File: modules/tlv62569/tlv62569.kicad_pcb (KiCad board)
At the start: 2 copper layers, 14.2 x 20.6 mm, 11 parts, among them U1 SMAJ17A, U2 TLV62569DBV

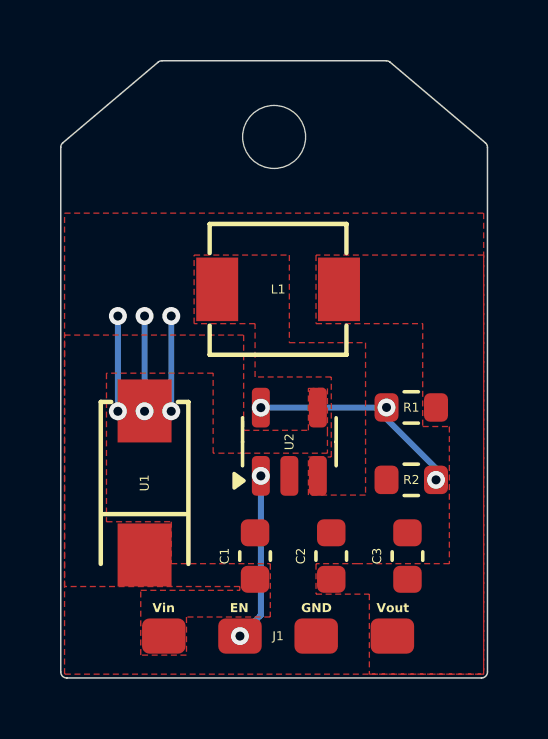
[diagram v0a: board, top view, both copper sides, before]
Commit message: Update `Notes` of `README.md` in module `tlv62569`
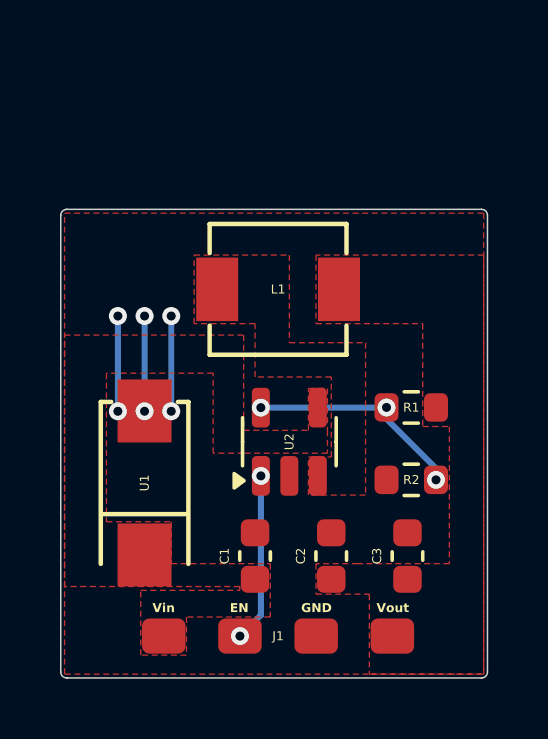
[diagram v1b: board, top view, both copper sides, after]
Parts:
- removed REF**: MountingHole_2.1mm, MountingHole:MountingHole_2.1mm
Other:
- board size 14.2 x 20.6 mm -> 14.2 x 15.6 mm
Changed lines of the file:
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@@
 		(at 130.9425 81.026 180)
 		(property "Reference" "L1"
-			(at 0 0 360)
+			(at 0 0 0)
 			(layer "F.SilkS")
 			(effects
@@
 		)
 		(property "Value" "2.2uH"
-			(at 0 4 360)
+			(at 0 4 0)
 			(layer "F.Fab")
 			(effects
@@
 		)
 		(property "Footprint" "easyeda2kicad:IND-SMD_L4.4-W4.2"
-			(at 0 0 360)
+			(at 0 0 0)
 			(layer "F.Fab")
 			(hide yes)
@@
 		)
 		(property "Datasheet" ""
-			(at 0 0 360)
+			(at 0 0 0)
 			(layer "F.Fab")
 			(hide yes)
@@
 		)
 		(property "Description" "Inductor"
-			(at 0 0 360)
+			(at 0 0 0)
 			(layer "F.Fab")
 			(hide yes)
@@
 		)
 		(fp_text user "${REFERENCE}"
-			(at 0 0 360)
+			(at 0 0 0)
 			(layer "F.Fab")
 			(effects
@@
 		)
 	)
-	(footprint "MountingHole:MountingHole_2.1mm"
-		(layer "F.Cu")
-		(at 130.81 75.946)
-		(descr "Mounting Hole 2.1mm, no annular")
-		(tags "mounting hole 2.1mm no annular")
-		(property "Reference" "REF**"
-			(at 0 -3.2 0)
-			(layer "F.SilkS")
-			(hide yes)
-			(effects
-				(font
-					(size 0.3 0.3)
-					(thickness 0.03)
-				)
-			)
-		)
-		(property "Value" "MountingHole_2.1mm"
-			(at 0 3.2 0)
-			(layer "F.Fab")
-			(effects
-				(font
-					(size 0.3 0.3)
-					(thickness 0.03)
-				)
-			)
-		)
-		(property "Footprint" "MountingHole:MountingHole_2.1mm"
-			(at 0 0 0)
-			(unlocked yes)
-			(layer "F.Fab")
-			(hide yes)
-			(effects
-				(font
-					(size 1.27 1.27)
-					(thickness 0.15)
-				)
-			)
-		)
-		(property "Datasheet" ""
-			(at 0 0 0)
-			(unlocked yes)
-			(layer "F.Fab")
-			(hide yes)
-			(effects
-				(font
-					(size 1.27 1.27)
-					(thickness 0.15)
-				)
-			)
-		)
-		(property "Description" ""
-			(at 0 0 0)
-			(unlocked yes)
-			(layer "F.Fab")
-			(hide yes)
-			(effects
-				(font
-					(size 1.27 1.27)
-					(thickness 0.15)
-				)
-			)
-		)
-		(attr exclude_from_pos_files exclude_from_bom)
-		(fp_circle
-			(center 0 0)
-			(end 2.1 0)
-			(stroke
-				(width 0.15)
-				(type solid)
-			)
-			(fill none)
-			(layer "Cmts.User")
-		)
-		(fp_circle
-			(center 0 0)
-			(end 2.35 0)
-			(stroke
-				(width 0.05)
-				(type solid)
-			)
-			(fill none)
-			(layer "F.CrtYd")
-		)
-		(fp_text user "${REFERENCE}"
-			(at 0 0 0)
-			(layer "F.Fab")
-			(effects
-				(font
-					(size 0.3 0.3)
-					(thickness 0.03)
-				)
-			)
-		)
-		(pad "" np_thru_hole circle
-			(at 0 0)
-			(size 2.1 2.1)
-			(drill 2.1)
-			(layers "*.Cu" "*.Mask")
-		)
-	)
 	(footprint "pad:Empty_01x04_Pad"
 		(layer "F.Cu")
@@
 		)
 		(property "Footprint" ""
-			(at 0 0 360)
+			(at 0 0 0)
 			(layer "B.Fab")
 			(hide yes)
@@
 		)
 		(property "Datasheet" ""
-			(at 0 0 360)
+			(at 0 0 0)
 			(layer "B.Fab")
 			(hide yes)
@@
 		)
 		(property "Description" ""
-			(at 0 0 360)
+			(at 0 0 0)
 			(layer "B.Fab")
 			(hide yes)
@@
 		)
 	)
-	(gr_line
-		(start 134.546738 73.406)
-		(end 127.073262 73.406)
-		(stroke
-			(width 0.05)
-			(type default)
-		)
-		(layer "Edge.Cuts")
-	)
 	(gr_arc
 		(start 137.922 93.78)
@@
 	)
 	(gr_arc
-		(start 137.851189 76.140083)
-		(mid 137.903436 76.208611)
-		(end 137.922 76.29276)
-		(stroke
-			(width 0.05)
-			(type default)
-		)
-		(layer "Edge.Cuts")
-	)
-	(gr_arc
 		(start 123.898 93.98)
 		(mid 123.756579 93.921421)
@@
 		(layer "Edge.Cuts")
 	)
-	(gr_line
-		(start 137.851189 76.140083)
-		(end 134.675927 73.453323)
+	(gr_arc
+		(start 123.698 78.559)
+		(mid 123.756579 78.417579)
+		(end 123.898 78.359)
 		(stroke
 			(width 0.05)
@@
 		(layer "Edge.Cuts")
 	)
-	(gr_arc
-		(start 134.546738 73.406)
-		(mid 134.615523 73.418215)
-		(end 134.675927 73.453323)
+	(gr_line
+		(start 137.922 93.78)
+		(end 137.922 78.559)
 		(stroke
 			(width 0.05)
@@
 	)
 	(gr_line
-		(start 126.944073 73.453323)
-		(end 123.768811 76.140083)
-		(stroke
-			(width 0.05)
-			(type default)
-		)
-		(layer "Edge.Cuts")
-	)
-	(gr_line
-		(start 137.922 93.78)
-		(end 137.922 76.29276)
-		(stroke
-			(width 0.05)
-			(type default)
-		)
-		(layer "Edge.Cuts")
-	)
-	(gr_line
-		(start 123.698 76.29276)
+		(start 123.698 78.559)
 		(end 123.698 93.78)
 		(stroke
@@
 		(layer "Edge.Cuts")
 	)
-	(gr_arc
-		(start 126.944073 73.453323)
-		(mid 127.004468 73.418191)
-		(end 127.073262 73.406)
+	(gr_line
+		(start 137.722 78.359)
+		(end 123.898 78.359)
 		(stroke
 			(width 0.05)
@@
 	)
 	(gr_arc
-		(start 123.698 76.29276)
-		(mid 123.716564 76.208611)
-		(end 123.768811 76.140083)
+		(start 137.722 78.359)
+		(mid 137.863421 78.417579)
+		(end 137.922 78.559)
 		(stroke
 			(width 0.05)
@@
 		(layer "Margin")
 	)
-	(gr_line
-		(start 123.825 93.653)
-		(end 123.825 78.486)
+	(gr_arc
+		(start 123.825 78.686)
+		(mid 123.883579 78.544579)
+		(end 124.025 78.486)
 		(stroke
 			(width 0.1)
@@
 	)
 	(gr_line
-		(start 123.825 78.486)
-		(end 137.795 78.486)
+		(start 123.825 93.653)
+		(end 123.825 78.686)
+		(stroke
+			(width 0.1)
+			(type default)
+		)
+		(layer "Margin")
+	)
+	(gr_line
+		(start 124.025 78.486)
+		(end 137.595 78.486)
+		(stroke
+			(width 0.1)
+			(type default)
+		)
+		(layer "Margin")
+	)
+	(gr_arc
+		(start 137.595 78.486)
+		(mid 137.736421 78.544579)
+		(end 137.795 78.686)
 		(stroke
 			(width 0.1)
@@
 	)
 	(gr_line
-		(start 137.795 78.486)
+		(start 137.795 78.686)
 		(end 137.795 93.653)
 		(stroke
@@
 		)
 	)
+	(dimension
+		(type aligned)
+		(layer "User.1")
+		(pts
+			(xy 137.922 93.98) (xy 123.698 93.98)
+		)
+		(height -1.524)
+		(gr_text "14.2240 mm"
+			(at 130.81 95.504 0)
+			(layer "User.1")
+			(effects
+				(font
+					(size 1 1)
+					(thickness 0.15)
+				)
+			)
+		)
+		(format
+			(prefix "")
+			(suffix "")
+			(units 3)
+			(units_format 1)
+			(precision 4)
+		)
+		(style
+			(thickness 0.1)
+			(arrow_length 1.27)
+			(text_position_mode 2)
+			(extension_height 0.58642)
+			(extension_offset 0.5) keep_text_aligned)
+	)
+	(dimension
+		(type aligned)
+		(layer "User.1")
+		(pts
+			(xy 137.922 78.359) (xy 137.922 93.98)
+		)
+		(height -1.143)
+		(gr_text "15.6210 mm"
+			(at 138.938 86.233 90)
+			(layer "User.1")
+			(effects
+				(font
+					(size 1 1)
+					(thickness 0.15)
+				)
+			)
+		)
+		(format
+			(prefix "")
+			(suffix "")
+			(units 3)
+			(units_format 1)
+			(precision 4)
+		)
+		(style
+			(thickness 0.1)
+			(arrow_length 1.27)
+			(text_position_mode 2)
+			(extension_height 0.58642)
+			(extension_offset 0.5) keep_text_aligned)
+	)
 	(via

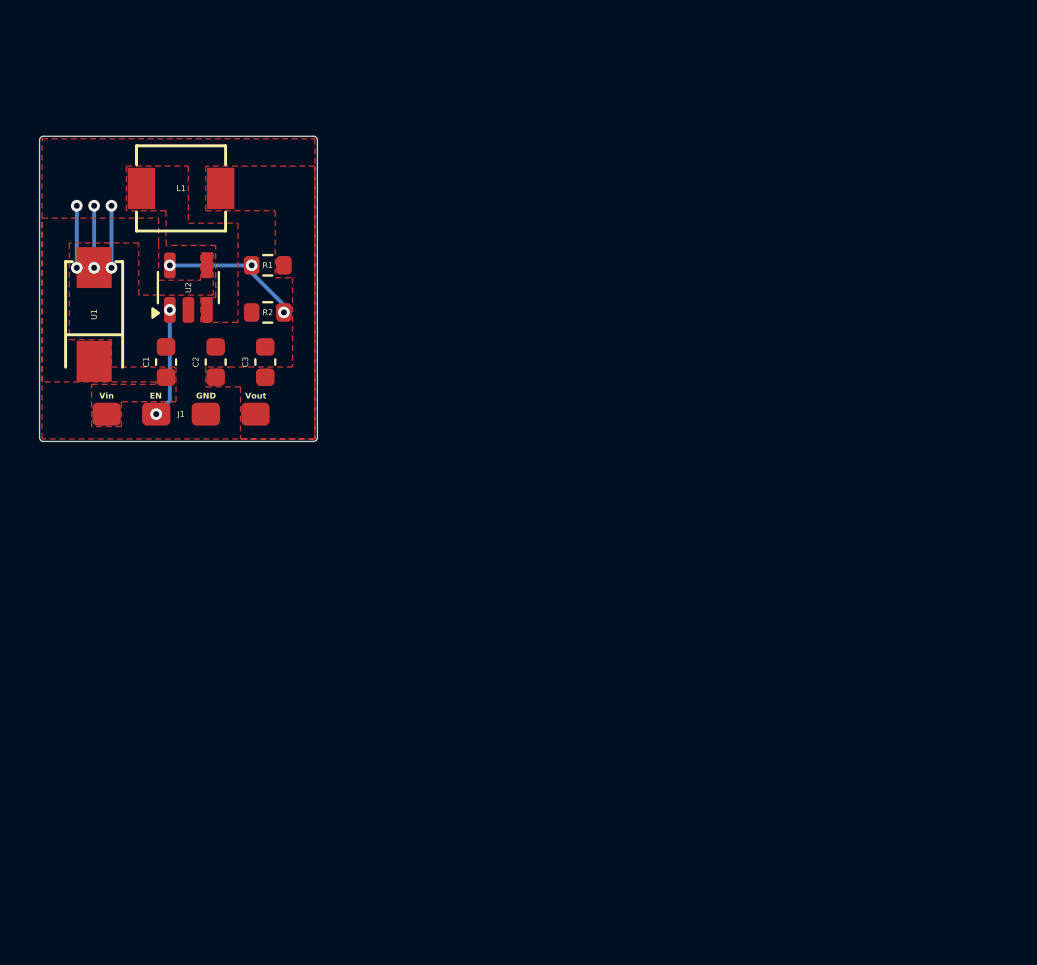
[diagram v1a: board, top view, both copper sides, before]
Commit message: Coppering for background of the module `tlv62569`
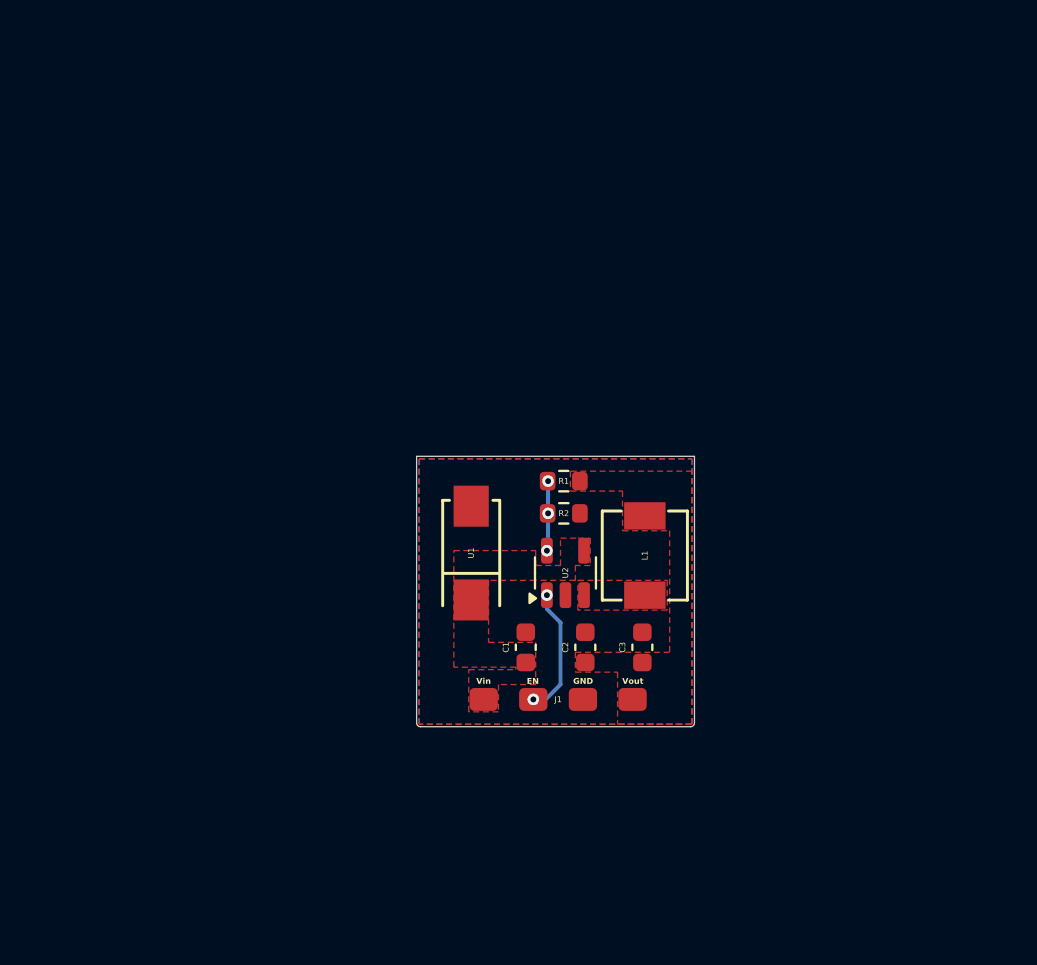
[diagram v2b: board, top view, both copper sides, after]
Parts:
- moved L1 30.3 mm to (154.7, 99.8), turned to -90 degrees
- moved C3 24.2 mm to (154.6, 104.5)
- moved G*** 24.2 mm to (146.9, 93.7)
- moved J1 24.2 mm to (150.2, 107.2)
- moved U2 24.2 mm to (150.6, 100.7)
- moved C2 23.9 mm to (151.6, 104.5)
- moved C1 23.5 mm to (148.6, 104.5)
- moved U1 22.8 mm to (145.8, 99.7)
- moved R1 18.8 mm to (150.5, 96.0)
- moved R2 18.3 mm to (150.5, 97.7), turned to 180 degrees
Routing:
- net GND: track 9.51 -> 0.00 mm, vias 6 -> 0
- net Net-(U2-FB): track 7.29 -> 3.65 mm
- net /EN: track 5.63 -> 6.57 mm
- added copper zone on B.Cu, net GND
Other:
- board size 14.2 x 15.6 mm -> 14.2 x 13.8 mm

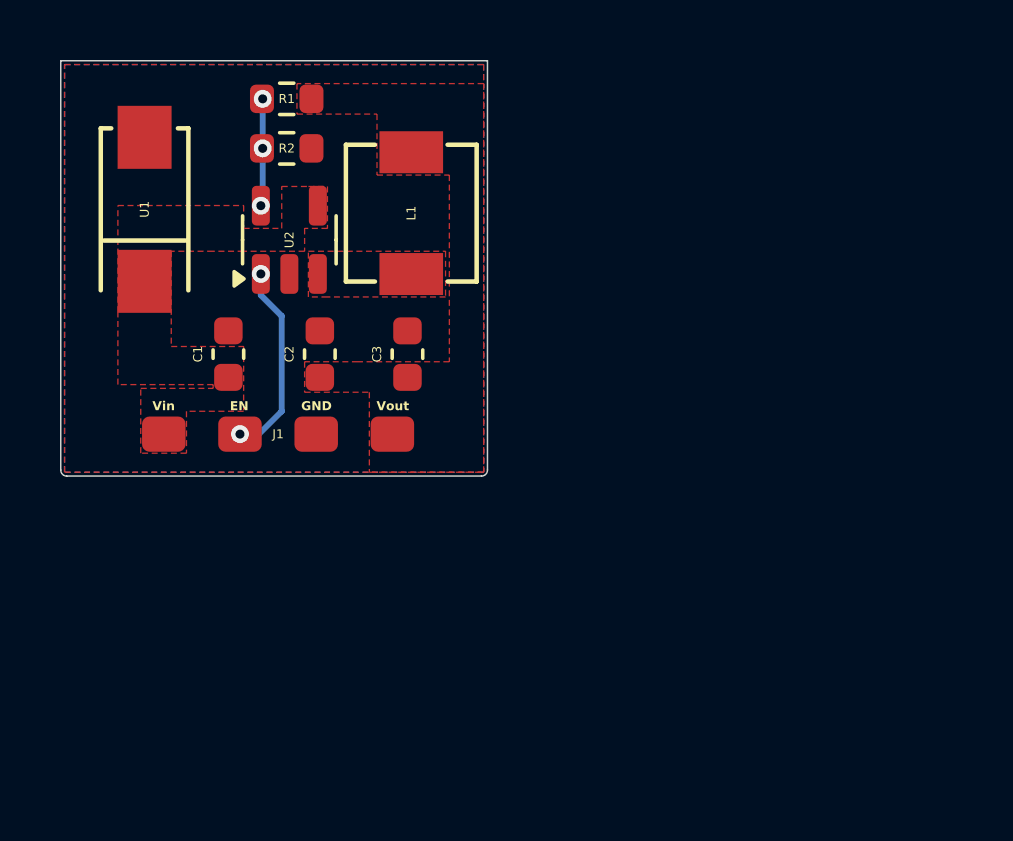
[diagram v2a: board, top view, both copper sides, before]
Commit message: Redesign `tlv62569` module
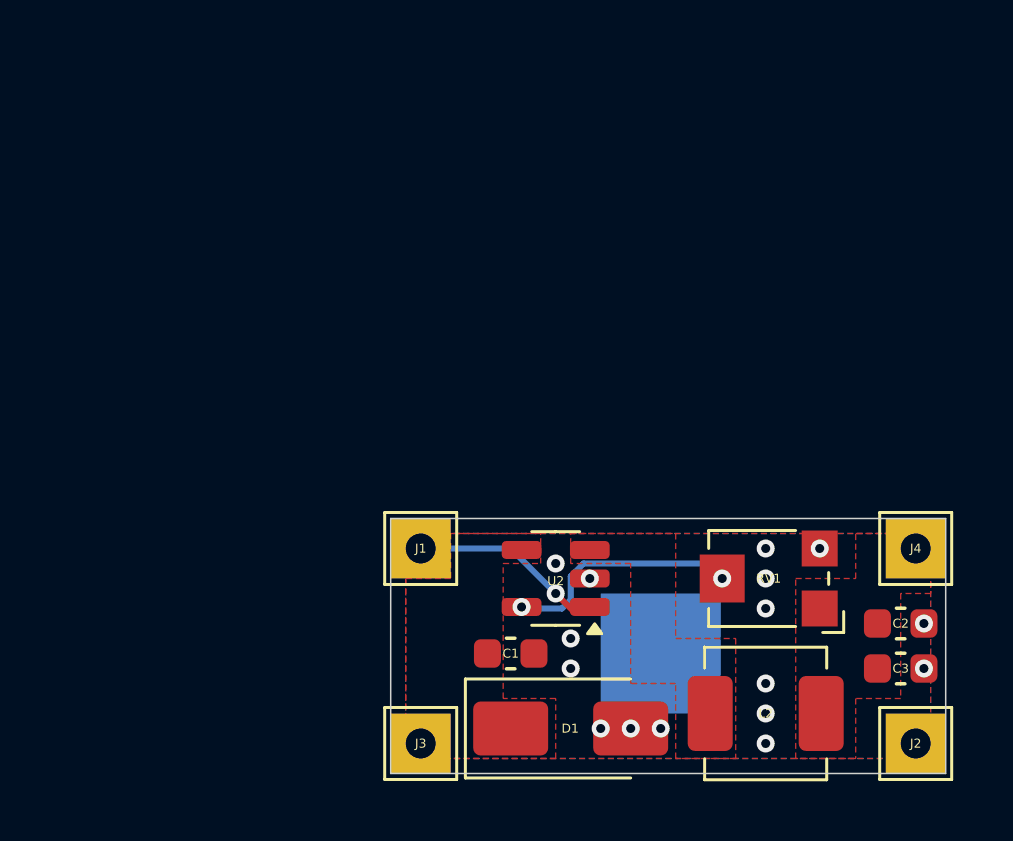
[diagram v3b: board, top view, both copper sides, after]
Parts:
- removed G***: LOGO, LOGO
- removed L1: 2.2uH, easyeda2kicad:IND-SMD_L4.4-W4.2
- removed R1, R2: R, Resistor_SMD:R_0603_1608Metric
- removed U1: SMAJ17A, easyeda2kicad:SMA_L4.3-W2.7-LS5.1-RD
- added D1: SMAJ17A, Diode_SMD:D_SMA, F.Cu at (160.0, 117.0)
- added J2: ~, TestPoint:TestPoint_THTPad_2.0x2.0mm_Drill1.0mm, F.Cu at (171.5, 117.5)
- added J3: ~, TestPoint:TestPoint_THTPad_2.0x2.0mm_Drill1.0mm, F.Cu at (155.0, 117.5)
- added J4: ~, TestPoint:TestPoint_THTPad_2.0x2.0mm_Drill1.0mm, F.Cu at (171.5, 111.0)
- added J5: ~, TestPoint:TestPoint_Pad_4.0x4.0mm, B.Cu at (163.0, 114.5)
- added L2: 2.2uH, Inductor_SMD:L_Changjiang_FXL0420, F.Cu at (166.5, 116.5)
- added RV1: 100k, Potentiometer_SMD:Potentiometer_Bourns_TC33X_Vertical, F.Cu at (166.5, 112.0)
- J1: footprint pad:Empty_01x04_Pad -> TestPoint:TestPoint_THTPad_2.0x2.0mm_Drill1.0mm
- moved C2 21.3 mm to (171.0, 113.5), turned to 180 degrees
- moved C3 19.5 mm to (171.0, 115.0), turned to 180 degrees
- moved U2 14.4 mm to (159.5, 112.0), turned to 180 degrees
- moved C1 13.7 mm to (158.0, 114.5), turned to 0 degrees
- moved J1 6.09 mm to (155.0, 111.0)
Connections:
- J1 pad 1: /Vin -> /EN
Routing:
- net Net-(U2-FB): track 3.65 -> 7.99 mm, vias 3 -> 2
- net /EN: track 6.57 -> 6.56 mm, vias 2 -> 1
- net GND: vias 0 -> 16
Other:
- board size 14.2 x 13.8 mm -> 18.5 x 8.5 mm
